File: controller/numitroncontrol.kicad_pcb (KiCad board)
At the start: 4 copper layers, 35 x 100 mm, 28 parts, among them J0 Screw_Terminal_01x02, J1 Conn_01x06, J2 Conn_01x06, J3 PTH, J3 RTC, J4 GPS, U1 LM317_TO-220

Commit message: fixed serial communication pins
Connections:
- net D_IN renamed D_IN1
- A1 pad D5: BLANKING -> D_IN2
- A1 pad D6: CLOCK -> BLANKING
- A1 pad D7: STROBE -> CLOCK
- A1 pad D8: unconnected-(A1-PadD8) -> STROBE
- J1 pad 2: Net-(J1-Pin_2) -> unconnected-(J1-Pin_2-Pad2)
- J2 pad 1: Net-(J1-Pin_2) -> D_IN2
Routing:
- net D_IN2: track 0.00 -> 47.4 mm
- net Net-(J1-Pin_2): track 14.9 -> 0.00 mm
- net +12V: track 104.3 -> 108.6 mm
- net CLOCK: track 68.8 -> 71.4 mm
- net BLANKING: track 71.2 -> 73.7 mm
- net D_IN1: track 34.5 -> 33.3 mm
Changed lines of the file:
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@@
 	(net 7 "unconnected-(A1-PadA3)")
 	(net 8 "unconnected-(A1-D2_INT0-PadD2)")
-	(net 9 "D_IN")
+	(net 9 "D_IN2")
 	(net 10 "unconnected-(A1-D12_MISO-PadD12)")
 	(net 11 "CLOCK")
@@
 	(net 16 "GND")
 	(net 17 "unconnected-(A1-D13_SCK-PadD13)")
-	(net 18 "unconnected-(A1-PadD8)")
+	(net 18 "D_IN1")
 	(net 19 "+5V")
 	(net 20 "+3V3")
@@
 	(net 29 "unconnected-(A1-PadD10)")
 	(net 30 "Net-(J0-Pin_1)")
-	(net 31 "Net-(J1-Pin_2)")
+	(net 31 "unconnected-(J1-Pin_2-Pad2)")
 	(net 32 "unconnected-(J2-Pin_2-Pad2)")
 	(net 33 "Net-(U1-ADJ)")
@@
 			(layers "*.Cu" "*.Mask")
 			(remove_unused_layers no)
-			(net 9 "D_IN")
+			(net 18 "D_IN1")
 			(pinfunction "Pin_1")
 			(pintype "passive")
@@
 			(layers "*.Cu" "*.Mask")
 			(remove_unused_layers no)
-			(net 31 "Net-(J1-Pin_2)")
+			(net 31 "unconnected-(J1-Pin_2-Pad2)")
 			(pinfunction "Pin_2")
 			(pintype "passive")
@@
 			(layer "F.Fab")
 		)
-		(fp_text user "D0"
-			(at 0 -36.83 90)
-			(unlocked yes)
-			(layer "B.SilkS")
-			(effects
-				(font
-					(size 1 1)
-					(thickness 0.15)
-				)
-				(justify mirror)
-			)
-		)
-		(fp_text user "D0"
-			(at 0 -36.83 90)
-			(unlocked yes)
-			(layer "F.SilkS")
-			(effects
-				(font
-					(size 1 1)
-					(thickness 0.15)
-				)
-			)
-		)
 		(fp_text user "USB"
 			(at 0 0.9525 0)
@@
 			(layers "*.Cu" "*.Mask")
 			(remove_unused_layers no)
-			(net 9 "D_IN")
+			(net 18 "D_IN1")
 			(pinfunction "D4")
 			(pintype "bidirectional")
@@
 			(layers "*.Cu" "*.Mask")
 			(remove_unused_layers no)
-			(net 2 "BLANKING")
+			(net 9 "D_IN2")
 			(pinfunction "D5")
 			(pintype "bidirectional")
@@
 			(layers "*.Cu" "*.Mask")
 			(remove_unused_layers no)
-			(net 11 "CLOCK")
+			(net 2 "BLANKING")
 			(pinfunction "D6")
 			(pintype "bidirectional")
@@
 			(layers "*.Cu" "*.Mask")
 			(remove_unused_layers no)
-			(net 14 "STROBE")
+			(net 11 "CLOCK")
 			(pinfunction "D7")
 			(pintype "bidirectional")
@@
 			(layers "*.Cu" "*.Mask")
 			(remove_unused_layers no)
-			(net 18 "unconnected-(A1-PadD8)")
+			(net 14 "STROBE")
 			(pinfunction "D8")
 			(pintype "bidirectional")
@@
 			(layers "*.Cu" "*.Mask")
 			(remove_unused_layers no)
-			(net 31 "Net-(J1-Pin_2)")
+			(net 9 "D_IN2")
 			(pinfunction "Pin_1")
 			(pintype "passive")
@@
 	)
 	(segment
-		(start 157.74 96.78)
-		(end 161 100.04)
+		(start 161 97.5)
+		(end 157.74 94.24)
 		(width 0.5)
 		(layer "B.Cu")
@@
 	)
 	(segment
-		(start 161 100.04)
-		(end 161 129.5)
+		(start 161 129.5)
+		(end 161 97.5)
 		(width 0.5)
 		(layer "B.Cu")
@@
 	)
 	(segment
-		(start 155 73.5)
-		(end 155 102.06)
-		(width 0.75)
-		(layer "In2.Cu")
-		(net 5)
-	)
-	(segment
-		(start 155 102.06)
-		(end 142.5 114.56)
+		(start 155 109.5)
+		(end 149.94 114.56)
 		(width 0.75)
 		(layer "In2.Cu")
@@
 	)
 	(segment
+		(start 149.94 114.56)
+		(end 142.5 114.56)
+		(width 0.75)
+		(layer "In2.Cu")
+		(net 5)
+	)
+	(segment
 		(start 155.5 125.08)
 		(end 153.81 126.77)
@@
 	)
 	(segment
-		(start 155.5 136.08)
-		(end 153.81 137.77)
+		(start 155 73.5)
+		(end 155 109.5)
 		(width 0.75)
 		(layer "In2.Cu")
@@
 	)
 	(segment
-		(start 144.915 125.495)
-		(end 144.915 110.085)
-		(width 0.5)
-		(layer "B.Cu")
-		(net 9)
+		(start 155.5 136.08)
+		(end 153.81 137.77)
+		(width 0.75)
+		(layer "In2.Cu")
+		(net 5)
 	)
 	(segment
-		(start 155.68 99.32)
-		(end 157.74 99.32)
+		(start 144.215 110.305)
+		(end 157.74 96.78)
 		(width 0.5)
 		(layer "B.Cu")
@@
 	)
 	(segment
-		(start 146.19 126.77)
-		(end 144.915 125.495)
+		(start 144.215 135.795)
+		(end 144.215 110.305)
 		(width 0.5)
 		(layer "B.Cu")
@@
 	)
 	(segment
-		(start 144.915 110.085)
-		(end 155.68 99.32)
+		(start 146.19 137.77)
+		(end 144.215 135.795)
 		(width 0.5)
 		(layer "B.Cu")
@@
 	)
 	(segment
-		(start 162 98.5)
-		(end 157.74 94.24)
+		(start 162 95.96)
+		(end 157.74 91.7)
 		(width 0.5)
 		(layer "B.Cu")
@@
 	(segment
 		(start 162 121.5)
-		(end 162 98.5)
+		(end 162 95.96)
 		(width 0.5)
 		(layer "B.Cu")
@@
 	)
 	(segment
-		(start 157.74 91.7)
-		(end 156.4264 93.0136)
-		(width 0.5)
-		(layer "B.Cu")
-		(net 14)
-	)
-	(segment
-		(start 156.4264 93.0136)
-		(end 156.5136 92.9264)
-		(width 0.5)
-		(layer "B.Cu")
-		(net 14)
-	)
-	(segment
-		(start 163 97.642289)
-		(end 163 99)
-		(width 0.5)
-		(layer "B.Cu")
-		(net 14)
-	)
-	(segment
-		(start 163 99)
-		(end 163 128.5)
-		(width 0.5)
-		(layer "B.Cu")
-		(net 14)
-	)
-	(segment
-		(start 158.284111 92.9264)
-		(end 163 97.642289)
+		(start 163 94.42)
+		(end 157.74 89.16)
 		(width 0.5)
 		(layer "B.Cu")
@@
 	)
 	(segment
-		(start 156.5136 92.9264)
-		(end 158.284111 92.9264)
+		(start 163 128.5)
+		(end 163 94.42)
 		(width 0.5)
 		(layer "B.Cu")
@@
 	)
 	(segment
+		(start 144.915 125.495)
+		(end 146.19 126.77)
+		(width 0.5)
+		(layer "B.Cu")
+		(net 18)
+	)
+	(segment
+		(start 157.74 99.32)
+		(end 144.915 112.145)
+		(width 0.5)
+		(layer "B.Cu")
+		(net 18)
+	)
+	(segment
+		(start 144.915 112.145)
+		(end 144.915 125.495)
+		(width 0.5)
+		(layer "B.Cu")
+		(net 18)
+	)
+	(segment
 		(start 145.5 103.94)
 		(end 142.5 106.94)
@@
 	)
 	(segment
-		(start 164 122.5)
-		(end 164 93)
+		(start 157.74 86.74)
+		(end 157.74 86.62)
 		(width 0.5)
 		(layer "B.Cu")
@@
 	)
 	(segment
-		(start 157.74 86.74)
-		(end 157.74 86.62)
+		(start 157.74 86.62)
+		(end 164 92.88)
 		(width 0.5)
 		(layer "B.Cu")
@@
 	)
 	(segment
-		(start 164 93)
-		(end 157.74 86.74)
+		(start 164 92.88)
+		(end 164 122.5)
 		(width 0.5)
 		(layer "B.Cu")
@@
 	)
 	(segment
-		(start 146.19 124.23)
-		(end 144.5 125.92)
-		(width 0.5)
-		(layer "F.Cu")
-		(net 31)
-	)
-	(segment
-		(start 144.5 125.92)
-		(end 144.5 136.08)
-		(width 0.5)
-		(layer "F.Cu")
-		(net 31)
-	)
-	(segment
-		(start 144.5 136.08)
-		(end 146.19 137.77)
-		(width 0.5)
-		(layer "F.Cu")
-		(net 31)
-	)
-	(segment

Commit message: updated control board
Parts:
- removed ? (x14): , 
- removed A1: Arduino_Nano_Socket, PCM_arduino-library:Arduino_Nano_Socket
- removed the J3 at (106.5, 84.3)
- removed J4: GPS, Connector_PinHeader_2.54mm:PinHeader_1x04_P2.54mm_Vertical
- removed J5: , Qwiic GPS - Titan X1 v10:1X01_NO_SILK
- added A2: Arduino_Nano_RP2040_Connect_Socket, PCM_arduino-library:Arduino_Nano_Every_Socket, F.Cu at (150.1, 75.2)
- moved J3 24.9 mm to (135.0, 107.4)
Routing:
- net SCL: track 34.2 -> 18.9 mm
- net SDA: track 33.7 -> 18.8 mm
- net +3V3: track 43.1 -> 31.5 mm

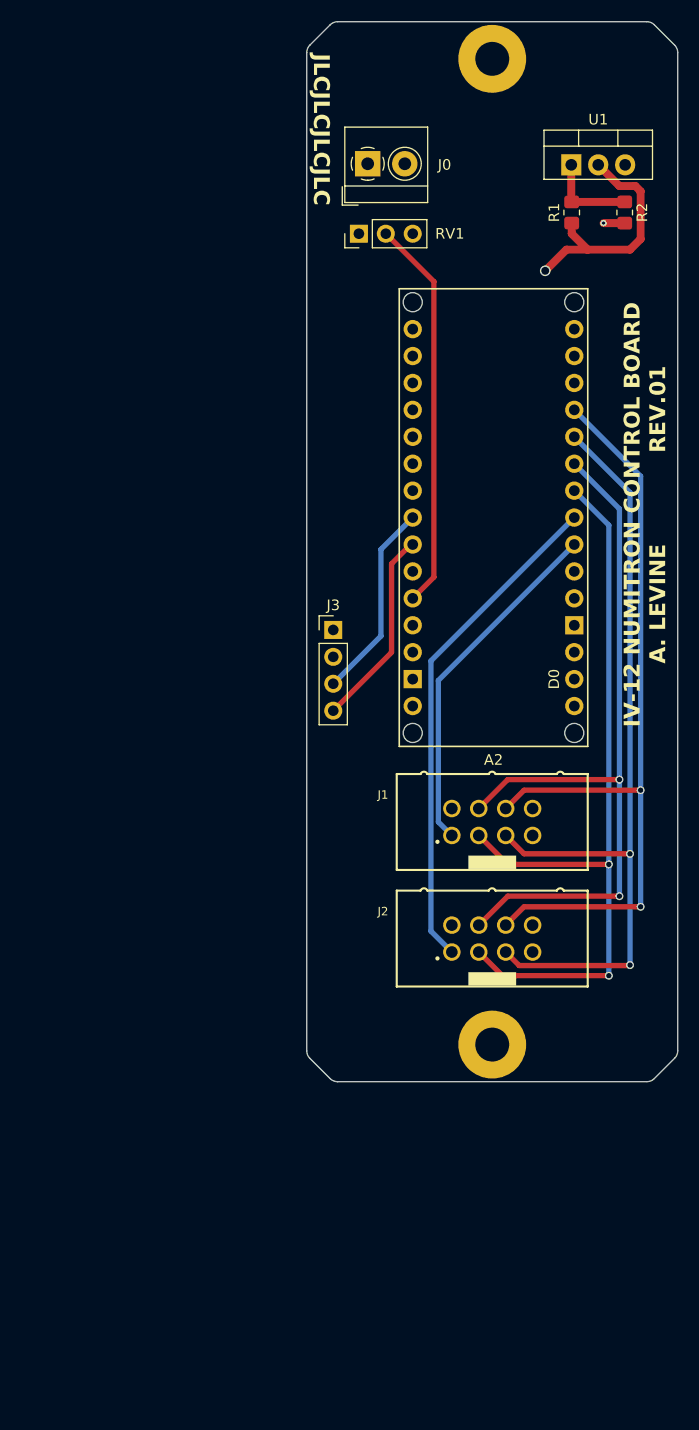
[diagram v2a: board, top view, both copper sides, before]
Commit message: replaced pot with screw terminal for flexible mounting
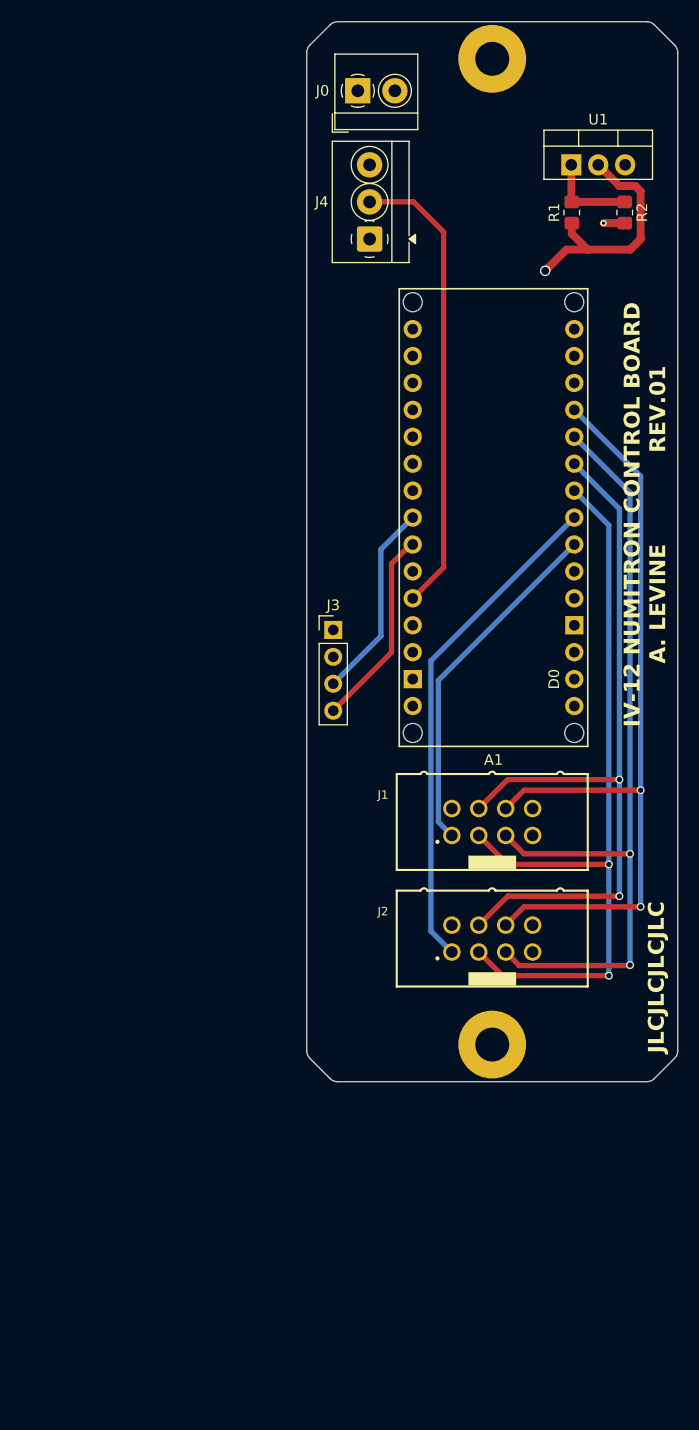
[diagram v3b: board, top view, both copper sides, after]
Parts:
- removed RV1: R_Potentiometer_US, Connector_PinHeader_2.54mm:PinHeader_1x03_P2.54mm_Vertical
- added J4: Screw_Terminal_01x03, TerminalBlock_4Ucon:TerminalBlock_4Ucon_1x03_P3.50mm_Horizontal, F.Cu at (138.4, 70.5)
- moved J0 6.95 mm to (137.3, 56.5)
- renumbered A2 to A1
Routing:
- net +5V: track 39.9 -> 0.00 mm
- net +3V3: track 31.5 -> 52.9 mm
- net POT: track 37.1 -> 43.9 mm
- net Net-(J0-Pin_1): track 26.3 -> 28.1 mm

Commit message: code attempt, small layout updates
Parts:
- moved J3 16.3 mm to (138.4, 91.4)
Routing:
- net +3V3: track 52.9 -> 37.0 mm
- net SCL: track 18.9 -> 4.18 mm
- net SDA: track 18.8 -> 4.18 mm
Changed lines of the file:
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@@
 	(net 2 "SDA")
 	(net 3 "+12V")
-	(net 4 "D_IN2")
+	(net 4 "D_IN1")
 	(net 5 "CLOCK")
 	(net 6 "STROBE")
 	(net 7 "GND")
-	(net 8 "D_IN1")
+	(net 8 "D_IN2")
 	(net 9 "+3V3")
 	(net 10 "DIMMING")
@@
 			(layers "*.Cu" "*.Mask")
 			(remove_unused_layers no)
-			(net 8 "D_IN1")
+			(net 4 "D_IN1")
 			(pinfunction "Pin_1")
 			(pintype "passive")
@@
 	(footprint "Connector_PinHeader_2.54mm:PinHeader_1x04_P2.54mm_Vertical"
 		(layer "F.Cu")
-		(at 135 107.38)
+		(at 138.43 91.44)
 		(descr "Through hole straight pin header, 1x04, 2.54mm pitch, single row")
 		(tags "Through hole pin header THT 1x04 2.54mm single row")
@@
 			(layers "*.Cu" "*.Mask")
 			(remove_unused_layers no)
-			(net 8 "D_IN1")
+			(net 4 "D_IN1")
 			(pinfunction "D4")
 			(pintype "bidirectional")
@@
 			(layers "*.Cu" "*.Mask")
 			(remove_unused_layers no)
-			(net 4 "D_IN2")
+			(net 8 "D_IN2")
 			(pinfunction "D5")
 			(pintype "bidirectional")
@@
 			(layers "*.Cu" "*.Mask")
 			(remove_unused_layers no)
-			(net 4 "D_IN2")
+			(net 8 "D_IN2")
 			(pinfunction "Pin_1")
 			(pintype "passive")
@@
 	(gr_arc
 		(start 132.5 52.914214)
-		(mid 132.576116 52.531528)
+		(mid 132.576122 52.531533)
 		(end 132.792893 52.207107)
 		(stroke
@@
 	(gr_arc
 		(start 134.707107 50.292893)
-		(mid 135.031531 50.076125)
+		(mid 135.031537 50.076146)
 		(end 135.414214 50)
 		(stroke
@@
 	(gr_arc
 		(start 165.292893 149.707107)
-		(mid 164.968469 149.923875)
+		(mid 164.968463 149.923854)
 		(end 164.585786 150)
 		(stroke
@@
 	(gr_arc
 		(start 132.792893 147.792893)
-		(mid 132.576125 147.468469)
+		(mid 132.576146 147.468463)
 		(end 132.5 147.085786)
 		(stroke
@@
 	(gr_arc
 		(start 164.585786 50)
-		(mid 164.968469 50.07612)
+		(mid 164.968472 50.076116)
 		(end 165.292893 50.292893)
 		(stroke
@@
 	(gr_arc
 		(start 167.207107 52.207107)
-		(mid 167.423875 52.531531)
+		(mid 167.423854 52.531537)
 		(end 167.5 52.914214)
 		(stroke
@@
 	(gr_arc
 		(start 135.414214 150)
-		(mid 135.031531 149.92388)
+		(mid 135.031528 149.923884)
 		(end 134.707107 149.707107)
 		(stroke
@@
 	(gr_arc
 		(start 167.5 147.085786)
-		(mid 167.42388 147.468469)
+		(mid 167.423884 147.468472)
 		(end 167.207107 147.792893)
 		(stroke
@@
 	)
 	(gr_text_box "1 GND\n2 3V3\n3 SDA\n4 SCL"
-		(start 133.505 117)
-		(end 137.005 121)
+		(start 136.68 100.87)
+		(end 140.18 104.87)
 		(margins 0.425 0.425 0.425 0.425)
 		(layer "F.SilkS")
@@
 	)
 	(segment
-		(start 139.5 99.78)
-		(end 139.5 107.96)
+		(start 138.69 96.78)
+		(end 138.43 96.52)
 		(width 0.5)
-		(layer "B.Cu")
-		(net 2)
-	)
-	(segment
-		(start 139.5 107.96)
-		(end 135 112.46)
-		(width 0.5)
-		(layer "B.Cu")
+		(layer "F.Cu")
 		(net 2)
 	)
 	(segment
 		(start 142.5 96.78)
-		(end 139.5 99.78)
+		(end 138.69 96.78)
 		(width 0.5)
-		(layer "B.Cu")
+		(layer "F.Cu")
 		(net 2)
 	)
@@
 	)
 	(segment
-		(start 144.215 110.305)
-		(end 157.74 96.78)
+		(start 146.19 126.77)
+		(end 144.914 125.494)
 		(width 0.5)
-		(layer "B.Cu")
+		(layer "F.Cu")
 		(net 4)
 	)
 	(segment
-		(start 144.215 135.795)
-		(end 144.215 110.305)
+		(start 144.914 112.146)
+		(end 157.74 99.32)
 		(width 0.5)
-		(layer "B.Cu")
+		(layer "F.Cu")
 		(net 4)
 	)
 	(segment
-		(start 146.19 137.77)
-		(end 144.215 135.795)
+		(start 144.914 125.494)
+		(end 144.914 112.146)
 		(width 0.5)
-		(layer "B.Cu")
+		(layer "F.Cu")
 		(net 4)
 	)
@@
 	)
 	(segment
-		(start 144.915 125.495)
-		(end 146.19 126.77)
+		(start 146.19 137.77)
+		(end 143.901 135.481)
 		(width 0.5)
-		(layer "B.Cu")
+		(layer "F.Cu")
 		(net 8)
 	)
 	(segment
-		(start 157.74 99.32)
-		(end 144.915 112.145)
+		(start 143.901 110.619)
+		(end 157.74 96.78)
 		(width 0.5)
-		(layer "B.Cu")
+		(layer "F.Cu")
 		(net 8)
 	)
 	(segment
-		(start 144.915 112.145)
-		(end 144.915 125.495)
+		(start 143.901 135.481)
+		(end 143.901 110.619)
 		(width 0.5)
-		(layer "B.Cu")
+		(layer "F.Cu")
 		(net 8)
 	)
@@
 	)
 	(segment
-		(start 136.525 87.515)
-		(end 136.525 108.585)
+		(start 138.43 93.98)
+		(end 136.525 92.075)
 		(width 0.5)
 		(layer "In2.Cu")
@@
 	)
 	(segment
-		(start 136.525 65.405)
-		(end 136.525 75.565)
+		(start 136.525 87.515)
+		(end 142.5 81.54)
 		(width 0.5)
 		(layer "In2.Cu")
@@
 	)
 	(segment
-		(start 142.5 81.54)
+		(start 136.525 92.075)
 		(end 136.525 87.515)
 		(width 0.5)
@@
 	)
 	(segment
-		(start 135.19 109.92)
-		(end 135 109.92)
-		(width 0.5)
-		(layer "In2.Cu")
-		(net 9)
-	)
-	(segment
-		(start 136.525 108.585)
-		(end 135.19 109.92)
+		(start 136.525 65.405)
+		(end 136.525 75.565)
 		(width 0.5)
 		(layer "In2.Cu")
@@
 	)
 	(segment
-		(start 140.5 101.14)
-		(end 140.5 109.5)
-		(width 0.5)
-		(layer "F.Cu")
-		(net 11)
-	)
-	(segment
 		(start 142.5 99.32)
-		(end 142.32 99.32)
-		(width 0.5)
-		(layer "F.Cu")
-		(net 11)
-	)
-	(segment
-		(start 142.32 99.32)
-		(end 140.5 101.14)
+		(end 138.69 99.32)
 		(width 0.5)
 		(layer "F.Cu")
@@
 	)
 	(segment
-		(start 140.5 109.5)
-		(end 135 115)
+		(start 138.69 99.32)
+		(end 138.43 99.06)
 		(width 0.5)
 		(layer "F.Cu")

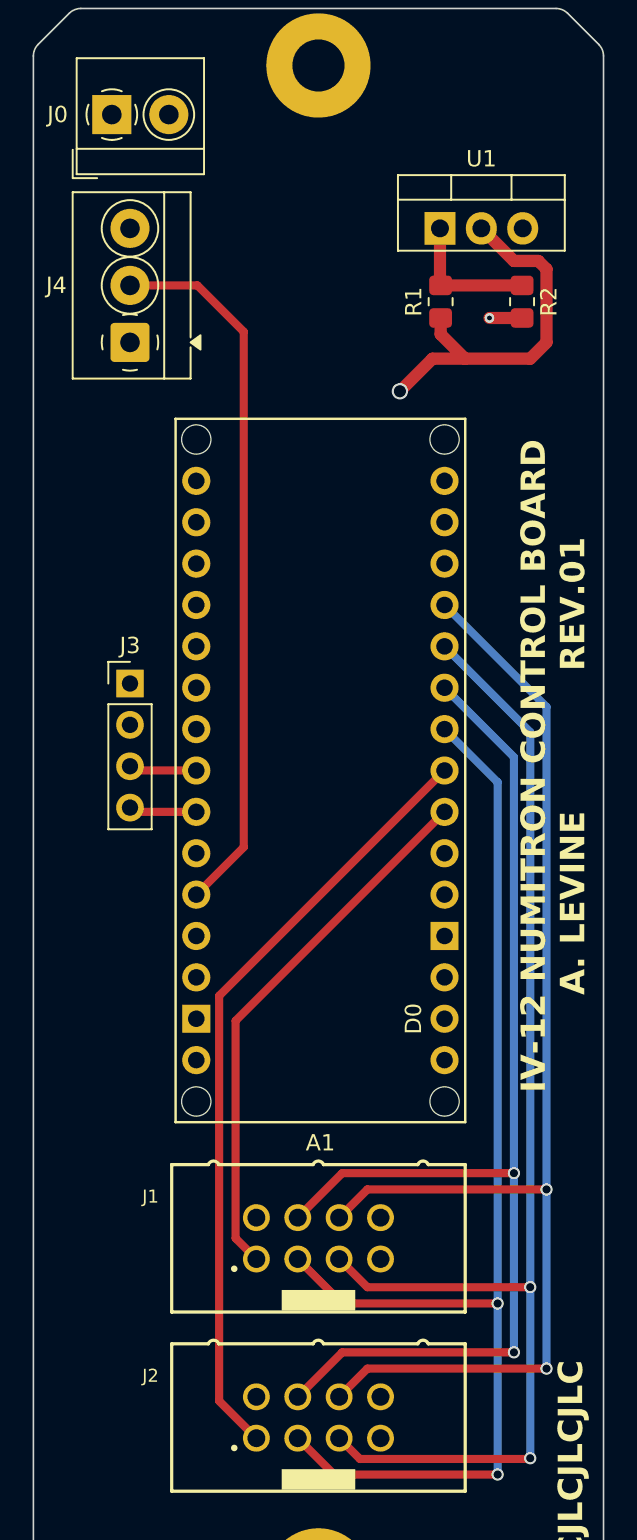
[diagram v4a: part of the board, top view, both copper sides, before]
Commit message: Added jumper for control schemes
can have discrete or daisy control of second output on control board
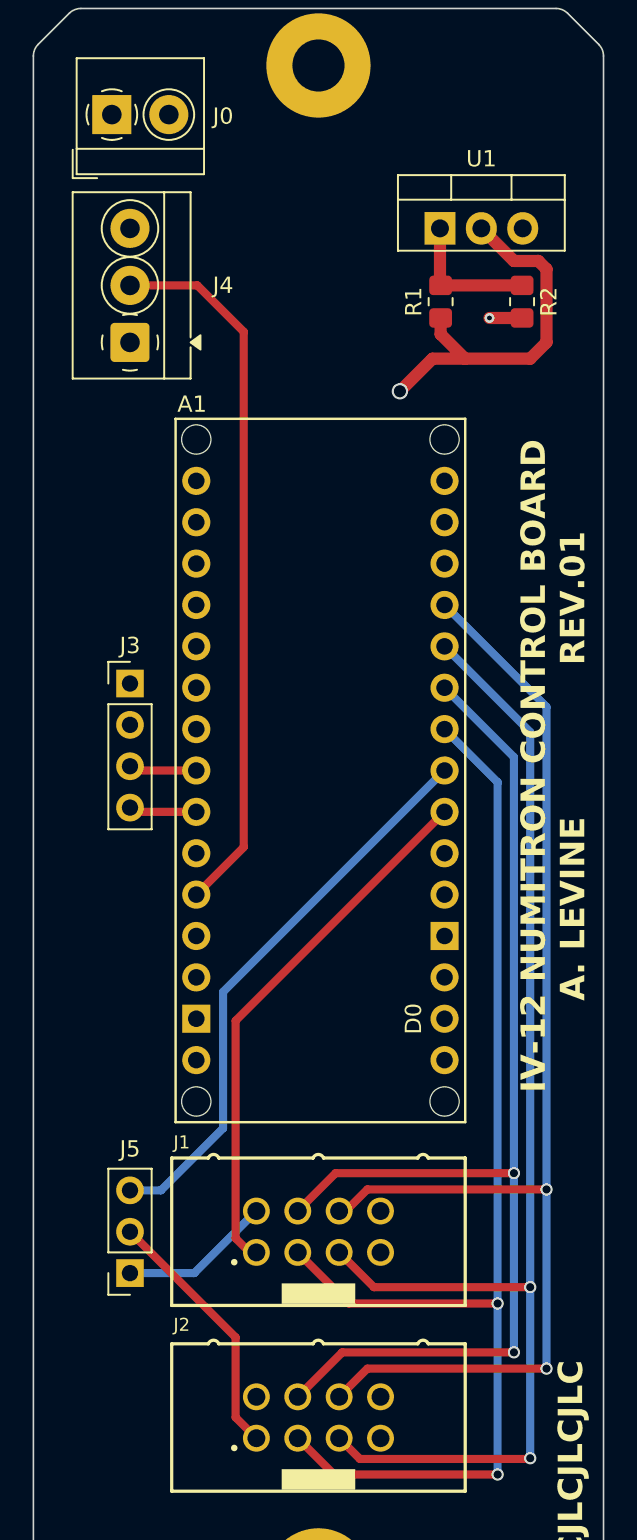
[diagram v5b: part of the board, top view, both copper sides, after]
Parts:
- added J5: Conn_01x03_Pin, Connector_PinSocket_2.54mm:PinSocket_1x03_P2.54mm_Vertical, F.Cu at (138.4, 127.6)
- moved J1 0.41 mm to (150.0, 125.1)
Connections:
- J1 pad 2: unconnected-(J1-Pin_2-Pad2) -> D_OUT1
- J2 pad 1: D_IN2 -> Net-(J2-Pin_1)
- J2 pad 2: unconnected-(J2-Pin_2-Pad2) -> D_OUT2
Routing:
- net Net-(J2-Pin_1): track 0.00 -> 15.9 mm
- net D_IN2: track 47.7 -> 34.9 mm
- net D_OUT1: track 0.00 -> 9.34 mm
- net +12V: track 108.6 -> 109.1 mm

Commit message: control board layout tweaks
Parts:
- J4: footprint TerminalBlock_4Ucon:TerminalBlock_4Ucon_1x03_P3.50mm_Horizontal -> Connector_PinHeader_2.54mm:PinHeader_1x03_P2.54mm_Vertical
- moved J4 78.1 mm to (114.3, 144.8), turned to 180 degrees
- moved J0 39.7 mm to (114.3, 88.9)
- moved J3 39.4 mm to (114.3, 122.6)
- moved J5 38.9 mm to (114.3, 158.1)
- moved J1 38.5 mm to (126.9, 155.9)
- moved J2 38.5 mm to (126.9, 167.3)
- moved REF** 38.5 mm to (126.9, 177.3)
- moved A1 38.5 mm to (127.0, 106.0)
- moved R1 38.5 mm to (134.4, 98.8)
- moved R2 38.5 mm to (139.4, 98.8)
- moved REF** 38.5 mm to (126.9, 84.3)
- moved U1 38.5 mm to (134.3, 94.3)
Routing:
- net POT: track 43.9 -> 8.90 mm
- net +3V3: track 37.0 -> 38.1 mm
- net Net-(J0-Pin_1): track 28.1 -> 27.3 mm
- net Net-(J2-Pin_1): track 15.9 -> 16.4 mm
- net D_OUT1: track 9.34 -> 9.84 mm
